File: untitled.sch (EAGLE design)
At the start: 21 parts

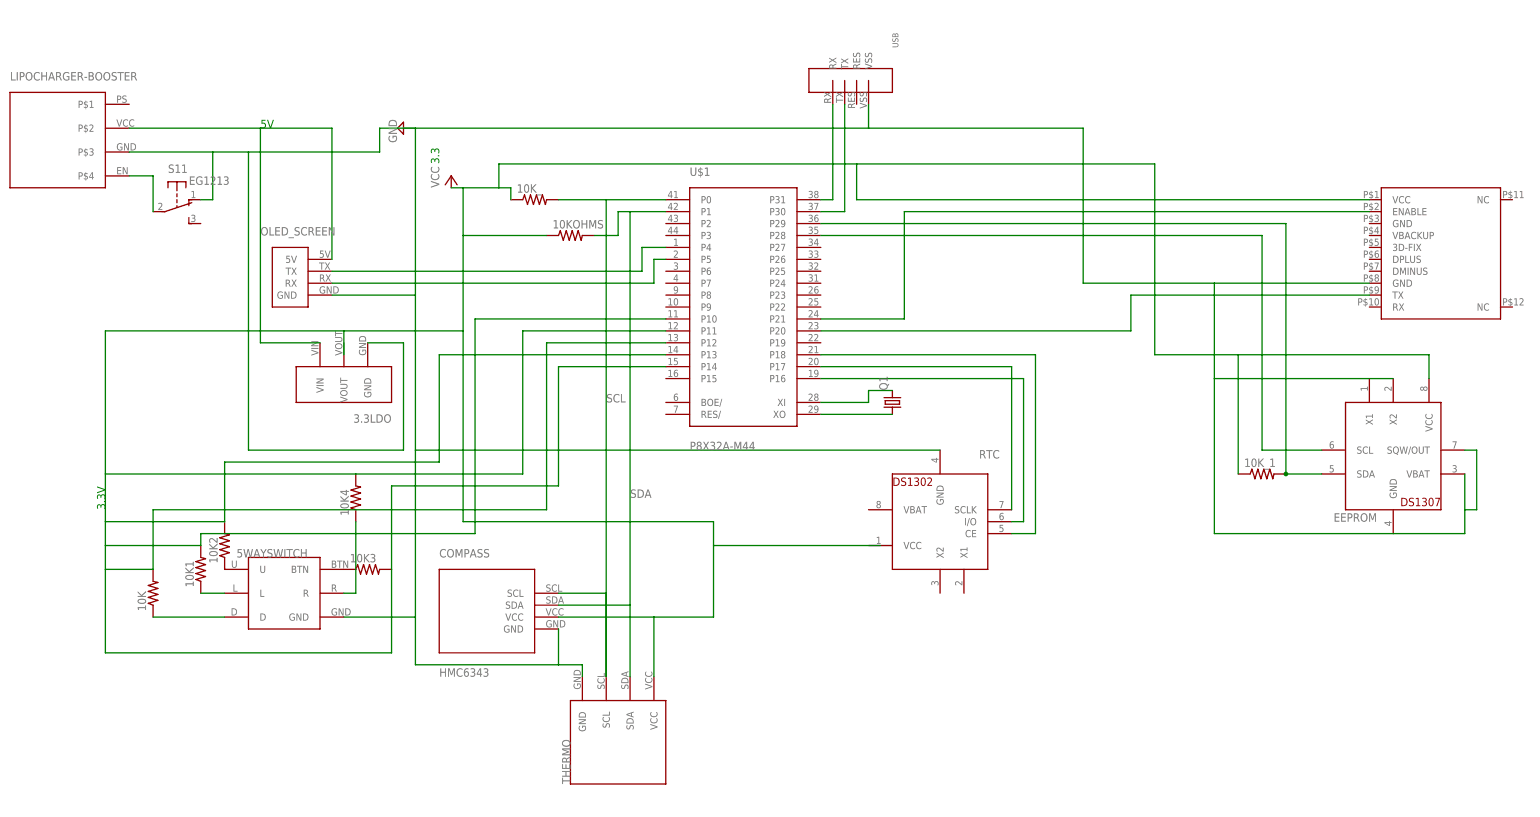
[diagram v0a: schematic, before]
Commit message: used sane resistors
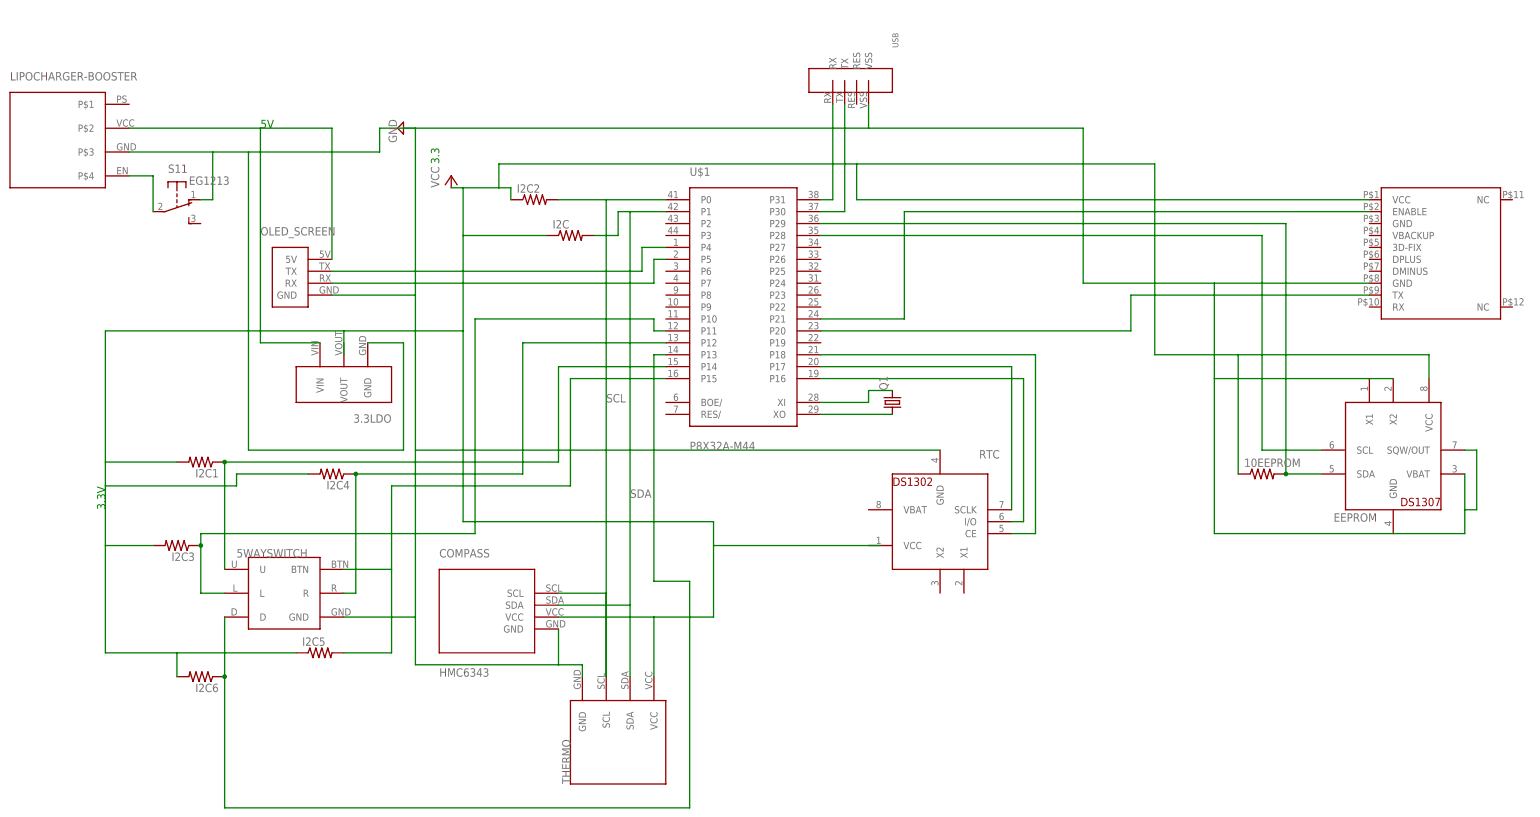
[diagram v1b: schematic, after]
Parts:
- removed 10K, 10K1, 10K2, 10K3, 10K4, 10KOHMS, 10K_, 10K_1: (no value), rcl:R-US_R0201
- added 10EEPROM, I2C, I2C1, I2C2, I2C3, I2C4, I2C5, I2C6: (no value), adafruit:R-US_R1005
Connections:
- removed net N$22: 10K2.1, 5WAYSWITCH.U
- removed net N$23: 10K3.1, 5WAYSWITCH.BTN
- removed net N$24: 10K4.1, 5WAYSWITCH.R
- new net N$14: 5WAYSWITCH.U, I2C1.1, U$1G$1.P14
- new net N$15: 5WAYSWITCH.D, I2C6.1, U$1G$1.P13
- new net N$17: 5WAYSWITCH.L, I2C3.1, U$1G$1.P11
- net N$18: now also 10EEPROM.2; no longer 10K_1.2
- net N$20: now also 5WAYSWITCH.R, I2C4.1, U$1G$1.P12; no longer 10K.1, 5WAYSWITCH.D
- net N$21: now also 5WAYSWITCH.BTN, I2C5.2, U$1G$1.P15; no longer 10K1.1, 5WAYSWITCH.L
- net SCL: now also I2C2.2; no longer 10K_.2
- net SDA: now also I2C.2; no longer 10KOHMS.2
- net VCC: now also 10EEPROM.1, I2C.1, I2C1.2, I2C2.1, I2C3.2, I2C4.2, I2C5.1, I2C6.2; no longer 10K.2, 10K1.2, 10K2.2, 10K3.2, 10K4.2, 10KOHMS.1, 10K_.1, 10K_1.1, U$1G$1.P10, U$1G$1.P11, U$1G$1.P12, U$1G$1.P13, U$1G$1.P14

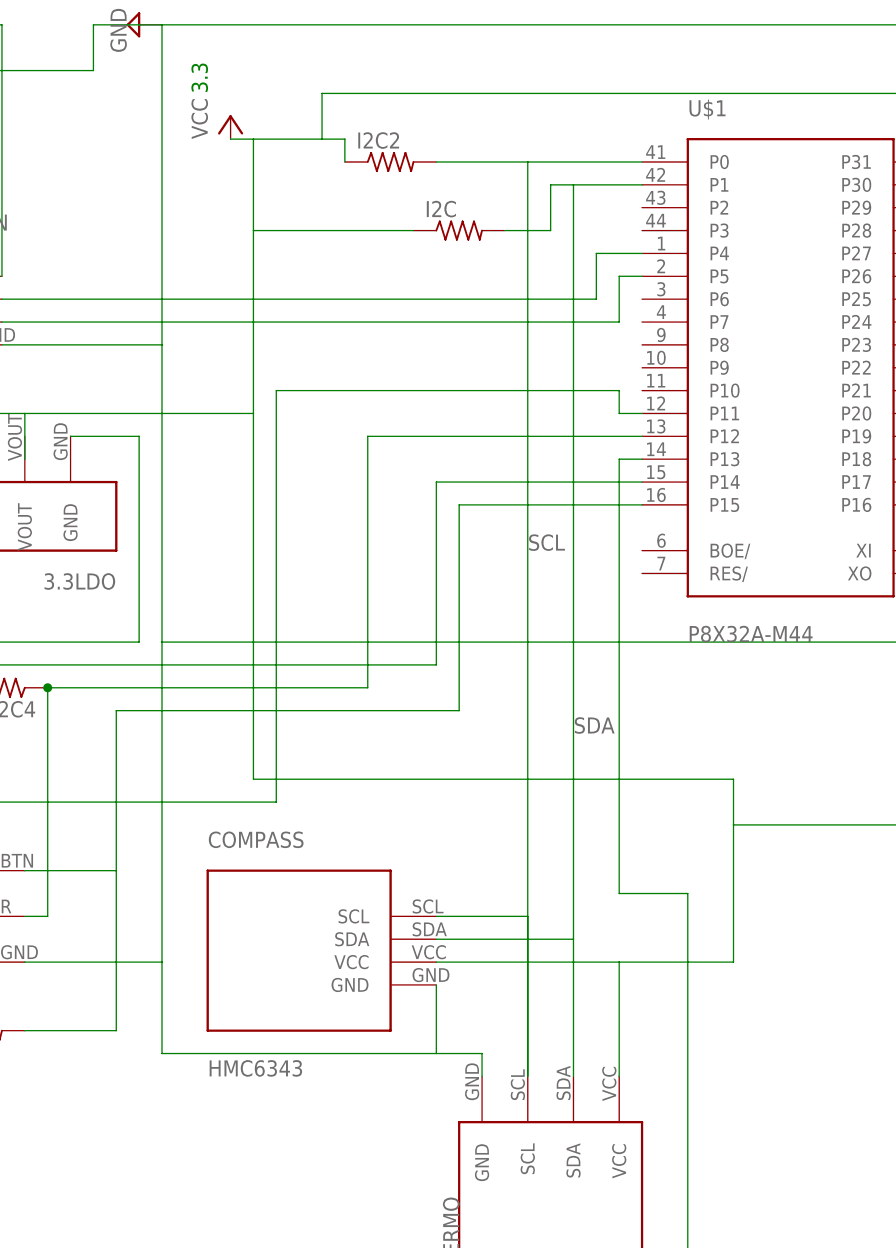
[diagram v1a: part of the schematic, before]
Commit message: replaced compass break out with raw part
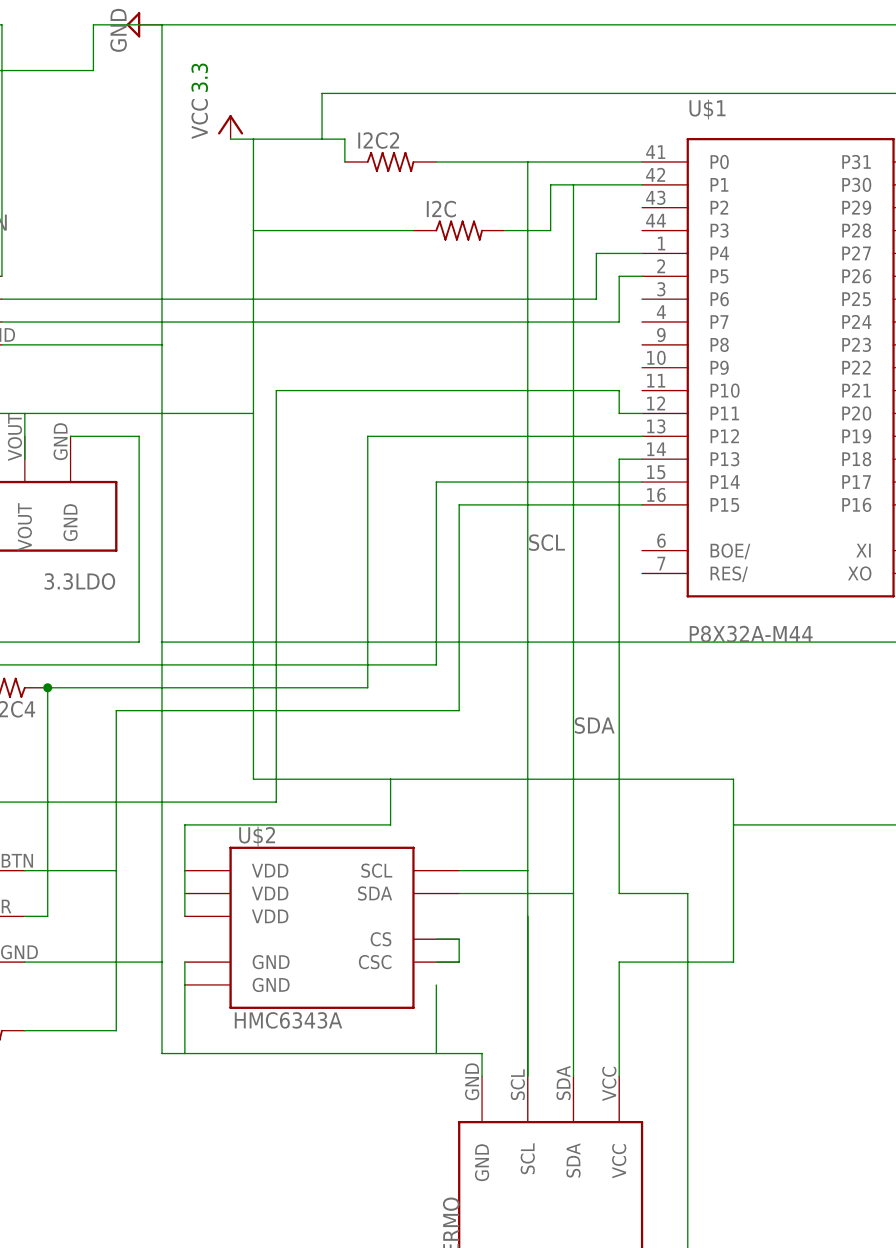
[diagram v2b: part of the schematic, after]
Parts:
- removed COMPASS: HMC6343, HMC6343Board:HMC6343
- added U$2: HMC6343A, SparkFun:HMC6343A
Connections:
- new net N$22: U$2.CS, U$2.CSC
- net GND: now also U$2.GND@25, U$2.GND@29; no longer COMPASS.GND
- net SCL: now also U$2.SCL; no longer COMPASS.SCL
- net SDA: now also U$2.SDA; no longer COMPASS.SDA
- net VCC: now also U$2.VDD@11, U$2.VDD@3; no longer COMPASS.VCC
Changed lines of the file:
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@@
 <part name="RTC" library="adafruit" deviceset="DS1302" device=""/>
 <part name="SUPPLY2" library="supply2" deviceset="GND" device=""/>
-<part name="COMPASS" library="HMC6343Board" deviceset="HMC6343" device=""/>
 <part name="THERMO" library="SFTemp" deviceset="SFTEMP" device=""/>
 <part name="P+1" library="supply1" deviceset="VCC" device=""/>
@@
 <part name="I2C6" library="adafruit" deviceset="R-US_" device="R1005"/>
 <part name="I2C1" library="adafruit" deviceset="R-US_" device="R1005"/>
+<part name="U$2" library="SparkFun" deviceset="HMC6343" device="A"/>
 </parts>
 <sheets>
@@
 <instance part="RTC" gate="G$1" x="68.58" y="15.24" rot="R180"/>
 <instance part="SUPPLY2" gate="GND" x="-45.72" y="99.06" rot="R270"/>
-<instance part="COMPASS" gate="G$1" x="-27.94" y="-2.54"/>
 <instance part="THERMO" gate="G$1" x="2.54" y="-30.48" rot="R90"/>
 <instance part="P+1" gate="VCC" x="-35.56" y="88.9"/>
@@
 <instance part="I2C6" gate="G$1" x="-88.9" y="-17.78" rot="R180"/>
 <instance part="I2C1" gate="G$1" x="-88.9" y="27.94" rot="R180"/>
+<instance part="U$2" gate="G$1" x="-25.4" y="0"/>
 </instances>
 <busses>
@@
 <wire x1="-43.18" y1="99.06" x2="53.34" y2="99.06" width="0.1524" layer="91"/>
 <wire x1="-43.18" y1="99.06" x2="-43.18" y2="63.5" width="0.1524" layer="91"/>
-<pinref part="COMPASS" gate="G$1" pin="GND"/>
 <wire x1="-43.18" y1="63.5" x2="-43.18" y2="30.48" width="0.1524" layer="91"/>
 <wire x1="-43.18" y1="30.48" x2="-43.18" y2="-5.08" width="0.1524" layer="91"/>
 <wire x1="-43.18" y1="-5.08" x2="-43.18" y2="-15.24" width="0.1524" layer="91"/>
-<wire x1="-43.18" y1="-15.24" x2="-12.7" y2="-15.24" width="0.1524" layer="91"/>
+<wire x1="-43.18" y1="-15.24" x2="-40.64" y2="-15.24" width="0.1524" layer="91"/>
+<wire x1="-40.64" y1="-15.24" x2="-12.7" y2="-15.24" width="0.1524" layer="91"/>
 <wire x1="-12.7" y1="-15.24" x2="-12.7" y2="-7.62" width="0.1524" layer="91"/>
 <wire x1="-12.7" y1="-15.24" x2="-7.62" y2="-15.24" width="0.1524" layer="91"/>
@@
 <wire x1="-88.9" y1="83.82" x2="-86.36" y2="83.82" width="0.1524" layer="91"/>
 <wire x1="-86.36" y1="83.82" x2="-86.36" y2="93.98" width="0.1524" layer="91"/>
+<pinref part="U$2" gate="G$1" pin="GND@29"/>
+<wire x1="-40.64" y1="-7.62" x2="-40.64" y2="-15.24" width="0.1524" layer="91"/>
+<pinref part="U$2" gate="G$1" pin="GND@25"/>
+<wire x1="-40.64" y1="-7.62" x2="-40.64" y2="-5.08" width="0.1524" layer="91"/>
 </segment>
 </net>
@@
 <wire x1="-12.7" y1="83.82" x2="-2.54" y2="83.82" width="0.1524" layer="91"/>
 <wire x1="10.16" y1="83.82" x2="-2.54" y2="83.82" width="0.1524" layer="91"/>
-<wire x1="-2.54" y1="83.82" x2="-2.54" y2="-17.78" width="0.1524" layer="91"/>
+<wire x1="-2.54" y1="83.82" x2="-2.54" y2="5.08" width="0.1524" layer="91"/>
 <label x="-2.54" y="40.64" size="1.778" layer="95"/>
-<pinref part="COMPASS" gate="G$1" pin="SCL"/>
-<wire x1="-12.7" y1="0" x2="-2.54" y2="0" width="0.1524" layer="91"/>
 <pinref part="THERMO" gate="G$1" pin="SCL"/>
+<wire x1="-2.54" y1="5.08" x2="-2.54" y2="-17.78" width="0.1524" layer="91"/>
 <wire x1="-2.54" y1="0" x2="-2.54" y2="-17.78" width="0.1524" layer="91"/>
 <pinref part="I2C2" gate="G$1" pin="2"/>
+<pinref part="U$2" gate="G$1" pin="SCL"/>
+<wire x1="-10.16" y1="5.08" x2="-2.54" y2="5.08" width="0.1524" layer="91"/>
 </segment>
 </net>
@@
 <wire x1="0" y1="76.2" x2="0" y2="81.28" width="0.1524" layer="91"/>
 <wire x1="0" y1="81.28" x2="2.54" y2="81.28" width="0.1524" layer="91"/>
-<wire x1="2.54" y1="81.28" x2="2.54" y2="-2.54" width="0.1524" layer="91"/>
+<wire x1="2.54" y1="81.28" x2="2.54" y2="2.54" width="0.1524" layer="91"/>
 <label x="2.54" y="20.32" size="1.778" layer="95"/>
-<pinref part="COMPASS" gate="G$1" pin="SDA"/>
-<wire x1="-12.7" y1="-2.54" x2="2.54" y2="-2.54" width="0.1524" layer="91"/>
-<wire x1="2.54" y1="-2.54" x2="2.54" y2="-17.78" width="0.1524" layer="91"/>
 <pinref part="THERMO" gate="G$1" pin="SDA"/>
 <pinref part="U$1" gate="G$1" pin="P1"/>
+<wire x1="2.54" y1="2.54" x2="2.54" y2="-17.78" width="0.1524" layer="91"/>
 <wire x1="10.16" y1="81.28" x2="2.54" y2="81.28" width="0.1524" layer="91"/>
 <pinref part="I2C" gate="G$1" pin="2"/>
+<pinref part="U$2" gate="G$1" pin="SDA"/>
+<wire x1="-10.16" y1="2.54" x2="2.54" y2="2.54" width="0.1524" layer="91"/>
 </segment>
 </net>
@@
 <wire x1="-33.02" y1="76.2" x2="-33.02" y2="55.88" width="0.1524" layer="91"/>
 <wire x1="-33.02" y1="55.88" x2="-33.02" y2="15.24" width="0.1524" layer="91"/>
-<wire x1="-33.02" y1="15.24" x2="20.32" y2="15.24" width="0.1524" layer="91"/>
+<wire x1="-33.02" y1="15.24" x2="-17.78" y2="15.24" width="0.1524" layer="91"/>
+<wire x1="-17.78" y1="15.24" x2="20.32" y2="15.24" width="0.1524" layer="91"/>
 <wire x1="20.32" y1="15.24" x2="20.32" y2="10.16" width="0.1524" layer="91"/>
 <wire x1="20.32" y1="10.16" x2="20.32" y2="-5.08" width="0.1524" layer="91"/>
@@
 <wire x1="114.3" y1="50.8" x2="114.3" y2="91.44" width="0.1524" layer="91"/>
 <wire x1="50.8" y1="91.44" x2="114.3" y2="91.44" width="0.1524" layer="91"/>
-<pinref part="COMPASS" gate="G$1" pin="VCC"/>
-<wire x1="7.62" y1="-5.08" x2="-12.7" y2="-5.08" width="0.1524" layer="91"/>
 <pinref part="10EEPROM" gate="G$1" pin="1"/>
 <pinref part="I2C2" gate="G$1" pin="1"/>
@@
 <pinref part="I2C5" gate="G$1" pin="1"/>
 <wire x1="-93.98" y1="-12.7" x2="-68.58" y2="-12.7" width="0.1524" layer="91"/>
+<pinref part="U$2" gate="G$1" pin="VDD@11"/>
+<pinref part="U$2" gate="G$1" pin="VDD@3"/>
+<wire x1="-40.64" y1="0" x2="-40.64" y2="5.08" width="0.1524" layer="91"/>
+<wire x1="-40.64" y1="5.08" x2="-40.64" y2="10.16" width="0.1524" layer="91"/>
+<wire x1="-40.64" y1="10.16" x2="-17.78" y2="10.16" width="0.1524" layer="91"/>
+<wire x1="-17.78" y1="10.16" x2="-17.78" y2="15.24" width="0.1524" layer="91"/>
 </segment>
 </net>
@@
 </segment>
 </net>
+<net name="N$22" class="0">
+<segment>
+<wire x1="-12.7" y1="-2.54" x2="-10.16" y2="-2.54" width="0.1524" layer="91"/>
+<pinref part="U$2" gate="G$1" pin="CS"/>
+<wire x1="-10.16" y1="-5.08" x2="-12.7" y2="-5.08" width="0.1524" layer="91"/>
+<pinref part="U$2" gate="G$1" pin="CSC"/>
+<wire x1="-10.16" y1="-2.54" x2="-10.16" y2="-5.08" width="0.1524" layer="91"/>
+</segment>
+</net>
